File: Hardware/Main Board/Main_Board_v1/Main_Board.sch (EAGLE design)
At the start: 59 parts, among them IC1 MBED_MICROCONTROLLER, IC2 LM311N, IC3 MCP602P, IC4 MCP602P, IC5 4072N, Q1 IRF3704, Q2 BS170

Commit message: Main Board Work in Progress
Work in Progress on the main board.
Need to test the timing circuit and then finalize and finish routing the
board.
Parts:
- removed R4, R5: (no value), rcl:R-EU_0411/12
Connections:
- net 5V_MBED: no longer R4.2, R5.2
- net P30: now also C6.1, IC4B.+IN, R16.2, U$8.1, U$8.2; no longer Q2.G
- net P36: now also Q2.G; no longer C6.1, IC4B.+IN, R16.2, U$8.1, U$8.2
- net SCL: no longer R5.1
- net SDA: no longer R4.1

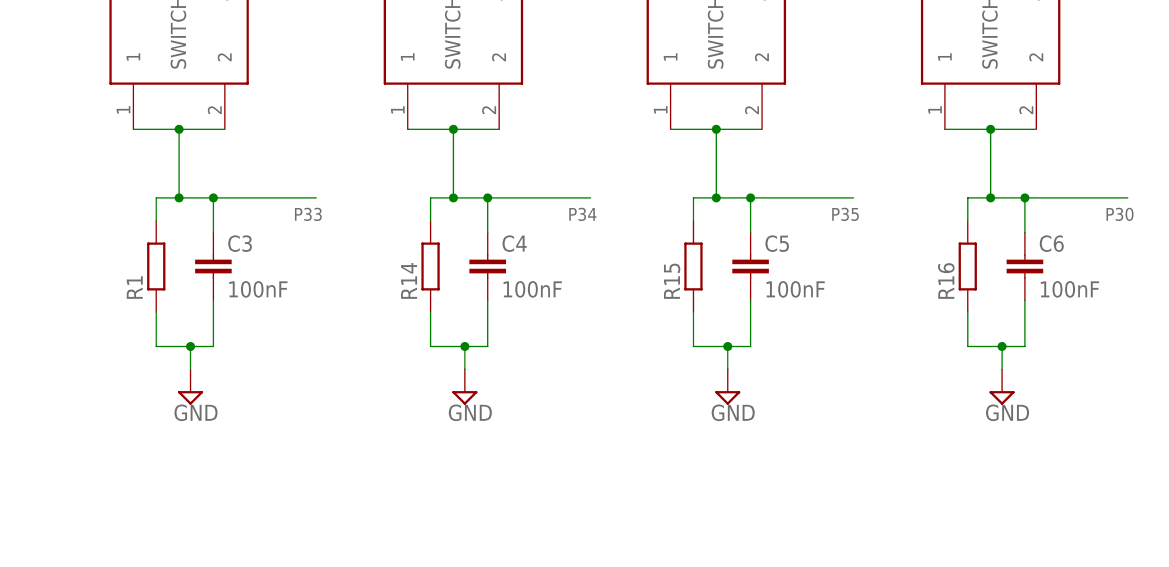
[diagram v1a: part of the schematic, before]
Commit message: Added Component Values for the AC Voltage sensor
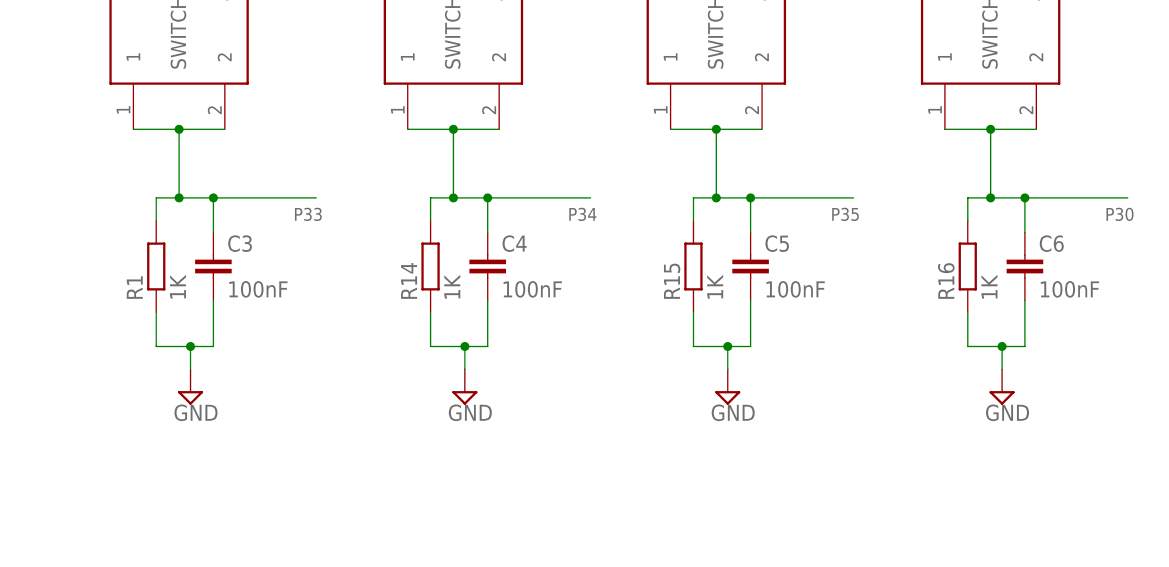
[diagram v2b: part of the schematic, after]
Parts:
- R1, R14, R15, R16: value (none) -> 1K
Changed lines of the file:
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@@
 <setting verticaltext="up"/>
 </settings>
-<grid distance="0.05" unitdist="inch" unit="inch" style="lines" multiple="1" display="yes" altdistance="0.025" altunitdist="inch" altunit="inch"/>
+<grid distance="0.1" unitdist="inch" unit="inch" style="lines" multiple="1" display="no" altdistance="0.01" altunitdist="inch" altunit="inch"/>
 <layers>
-<layer number="1" name="Top" color="4" fill="1" visible="yes" active="no"/>
-<layer number="2" name="Route2" color="1" fill="3" visible="yes" active="no"/>
-<layer number="3" name="Route3" color="4" fill="3" visible="yes" active="no"/>
-<layer number="4" name="Route4" color="1" fill="4" visible="yes" active="no"/>
-<layer number="5" name="Route5" color="4" fill="4" visible="yes" active="no"/>
-<layer number="6" name="Route6" color="1" fill="8" visible="yes" active="no"/>
-<layer number="7" name="Route7" color="4" fill="8" visible="yes" active="no"/>
-<layer number="8" name="Route8" color="1" fill="2" visible="yes" active="no"/>
-<layer number="9" name="Route9" color="4" fill="2" visible="yes" active="no"/>
-<layer number="10" name="Route10" color="1" fill="7" visible="yes" active="no"/>
-<layer number="11" name="Route11" color="4" fill="7" visible="yes" active="no"/>
-<layer number="12" name="Route12" color="1" fill="5" visible="yes" active="no"/>
-<layer number="13" name="Route13" color="4" fill="5" visible="yes" active="no"/>
-<layer number="14" name="Route14" color="1" fill="6" visible="yes" active="no"/>
-<layer number="15" name="Route15" color="4" fill="6" visible="yes" active="no"/>
-<layer number="16" name="Bottom" color="1" fill="1" visible="yes" active="no"/>
-<layer number="17" name="Pads" color="2" fill="1" visible="yes" active="no"/>
-<layer number="18" name="Vias" color="2" fill="1" visible="yes" active="no"/>
-<layer number="19" name="Unrouted" color="6" fill="1" visible="yes" active="no"/>
-<layer number="20" name="Dimension" color="15" fill="1" visible="yes" active="no"/>
-<layer number="21" name="tPlace" color="7" fill="1" visible="yes" active="no"/>
-<layer number="22" name="bPlace" color="7" fill="1" visible="yes" active="no"/>
-<layer number="23" name="tOrigins" color="15" fill="1" visible="yes" active="no"/>
-<layer number="24" name="bOrigins" color="15" fill="1" visible="yes" active="no"/>
-<layer number="25" name="tNames" color="7" fill="1" visible="yes" active="no"/>
-<layer number="26" name="bNames" color="7" fill="1" visible="yes" active="no"/>
-<layer number="27" name="tValues" color="7" fill="1" visible="yes" active="no"/>
-<layer number="28" name="bValues" color="7" fill="1" visible="yes" active="no"/>
+<layer number="1" name="Top" color="4" fill="1" visible="no" active="no"/>
+<layer number="2" name="Route2" color="1" fill="3" visible="no" active="no"/>
+<layer number="3" name="Route3" color="4" fill="3" visible="no" active="no"/>
+<layer number="4" name="Route4" color="1" fill="4" visible="no" active="no"/>
+<layer number="5" name="Route5" color="4" fill="4" visible="no" active="no"/>
+<layer number="6" name="Route6" color="1" fill="8" visible="no" active="no"/>
+<layer number="7" name="Route7" color="4" fill="8" visible="no" active="no"/>
+<layer number="8" name="Route8" color="1" fill="2" visible="no" active="no"/>
+<layer number="9" name="Route9" color="4" fill="2" visible="no" active="no"/>
+<layer number="10" name="Route10" color="1" fill="7" visible="no" active="no"/>
+<layer number="11" name="Route11" color="4" fill="7" visible="no" active="no"/>
+<layer number="12" name="Route12" color="1" fill="5" visible="no" active="no"/>
+<layer number="13" name="Route13" color="4" fill="5" visible="no" active="no"/>
+<layer number="14" name="Route14" color="1" fill="6" visible="no" active="no"/>
+<layer number="15" name="Route15" color="4" fill="6" visible="no" active="no"/>
+<layer number="16" name="Bottom" color="1" fill="1" visible="no" active="no"/>
+<layer number="17" name="Pads" color="2" fill="1" visible="no" active="no"/>
+<layer number="18" name="Vias" color="2" fill="1" visible="no" active="no"/>
+<layer number="19" name="Unrouted" color="6" fill="1" visible="no" active="no"/>
+<layer number="20" name="Dimension" color="15" fill="1" visible="no" active="no"/>
+<layer number="21" name="tPlace" color="7" fill="1" visible="no" active="no"/>
+<layer number="22" name="bPlace" color="7" fill="1" visible="no" active="no"/>
+<layer number="23" name="tOrigins" color="15" fill="1" visible="no" active="no"/>
+<layer number="24" name="bOrigins" color="15" fill="1" visible="no" active="no"/>
+<layer number="25" name="tNames" color="7" fill="1" visible="no" active="no"/>
+<layer number="26" name="bNames" color="7" fill="1" visible="no" active="no"/>
+<layer number="27" name="tValues" color="7" fill="1" visible="no" active="no"/>
+<layer number="28" name="bValues" color="7" fill="1" visible="no" active="no"/>
 <layer number="29" name="tStop" color="7" fill="3" visible="no" active="no"/>
 <layer number="30" name="bStop" color="7" fill="6" visible="no" active="no"/>
@@
 <layer number="35" name="tGlue" color="7" fill="4" visible="no" active="no"/>
 <layer number="36" name="bGlue" color="7" fill="5" visible="no" active="no"/>
-<layer number="37" name="tTest" color="7" fill="1" visible="yes" active="no"/>
-<layer number="38" name="bTest" color="7" fill="1" visible="yes" active="no"/>
+<layer number="37" name="tTest" color="7" fill="1" visible="no" active="no"/>
+<layer number="38" name="bTest" color="7" fill="1" visible="no" active="no"/>
 <layer number="39" name="tKeepout" color="4" fill="11" visible="no" active="no"/>
 <layer number="40" name="bKeepout" color="1" fill="11" visible="no" active="no"/>
@@
 <layer number="44" name="Drills" color="7" fill="1" visible="no" active="no"/>
 <layer number="45" name="Holes" color="7" fill="1" visible="no" active="no"/>
-<layer number="46" name="Milling" color="3" fill="1" visible="yes" active="no"/>
-<layer number="47" name="Measures" color="7" fill="1" visible="yes" active="no"/>
-<layer number="48" name="Document" color="7" fill="1" visible="yes" active="no"/>
-<layer number="49" name="Reference" color="7" fill="1" visible="yes" active="no"/>
-<layer number="50" name="dxf" color="7" fill="1" visible="yes" active="no"/>
-<layer number="51" name="tDocu" color="7" fill="1" visible="yes" active="no"/>
-<layer number="52" name="bDocu" color="7" fill="1" visible="yes" active="no"/>
-<layer number="53" name="tGND_GNDA" color="7" fill="1" visible="yes" active="no"/>
-<layer number="54" name="bGND_GNDA" color="7" fill="1" visible="yes" active="no"/>
-<layer number="56" name="wert" color="7" fill="1" visible="yes" active="no"/>
+<layer number="46" name="Milling" color="3" fill="1" visible="no" active="no"/>
+<layer number="47" name="Measures" color="7" fill="1" visible="no" active="no"/>
+<layer number="48" name="Document" color="7" fill="1" visible="no" active="no"/>
+<layer number="49" name="Reference" color="7" fill="1" visible="no" active="no"/>
+<layer number="50" name="dxf" color="7" fill="1" visible="no" active="no"/>
+<layer number="51" name="tDocu" color="7" fill="1" visible="no" active="no"/>
+<layer number="52" name="bDocu" color="7" fill="1" visible="no" active="no"/>
+<layer number="53" name="tGND_GNDA" color="7" fill="1" visible="no" active="no"/>
+<layer number="54" name="bGND_GNDA" color="7" fill="1" visible="no" active="no"/>
+<layer number="56" name="wert" color="7" fill="1" visible="no" active="no"/>
 <layer number="91" name="Nets" color="2" fill="1" visible="yes" active="yes"/>
 <layer number="92" name="Busses" color="1" fill="1" visible="yes" active="yes"/>
@@
 <part name="JP3" library="jumper" deviceset="JP10Q" device="" value="JP3"/>
 <part name="JP4" library="jumper" deviceset="JP10Q" device="" value="JP4"/>
-<part name="R1" library="rcl" deviceset="R-EU_" device="0411/12"/>
+<part name="R1" library="rcl" deviceset="R-EU_" device="0411/12" value="1K"/>
 <part name="C1" library="capacitor-wima" deviceset="C" device="5/3" value="100nF"/>
 <part name="R2" library="rcl" deviceset="R-EU_" device="0411/12"/>
@@
 <part name="POWER_SUPPLY" library="ekohub2013" deviceset="TRACO_ISOLATED_SUPPLY" device=""/>
 <part name="U$5" library="ekohub2013" deviceset="TACT_SWITCH" device=""/>
-<part name="R14" library="rcl" deviceset="R-EU_" device="0411/12"/>
+<part name="R14" library="rcl" deviceset="R-EU_" device="0411/12" value="1K"/>
 <part name="C4" library="capacitor-wima" deviceset="C" device="5/3" value="100nF"/>
 <part name="U$6" library="ekohub2013" deviceset="TACT_SWITCH" device=""/>
-<part name="R15" library="rcl" deviceset="R-EU_" device="0411/12"/>
+<part name="R15" library="rcl" deviceset="R-EU_" device="0411/12" value="1K"/>
 <part name="C5" library="capacitor-wima" deviceset="C" device="5/3" value="100nF"/>
 <part name="U$7" library="ekohub2013" deviceset="TACT_SWITCH" device=""/>
-<part name="R16" library="rcl" deviceset="R-EU_" device="0411/12"/>
+<part name="R16" library="rcl" deviceset="R-EU_" device="0411/12" value="1K"/>
 <part name="C6" library="capacitor-wima" deviceset="C" device="5/3" value="100nF"/>
 <part name="U$8" library="ekohub2013" deviceset="TACT_SWITCH" device=""/>
